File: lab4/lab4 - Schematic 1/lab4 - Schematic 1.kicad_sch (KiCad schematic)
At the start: 6 parts, among them SW1 SW_SPDT

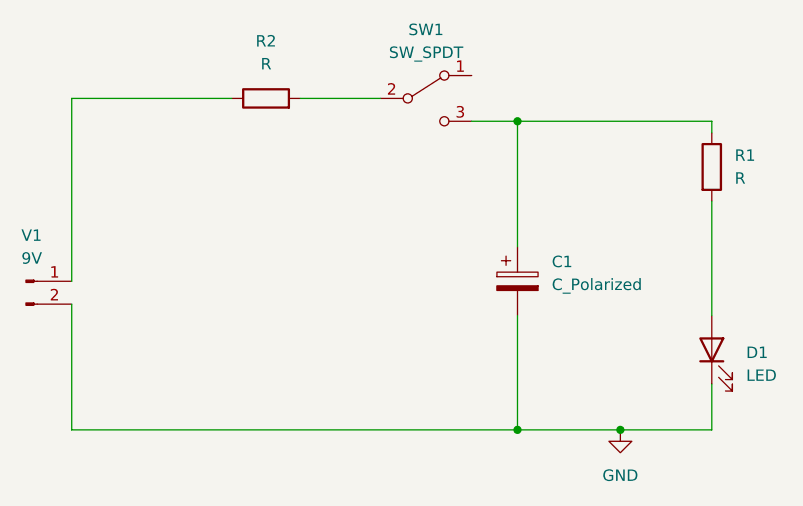
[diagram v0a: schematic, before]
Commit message: PCB for first schematic is complete
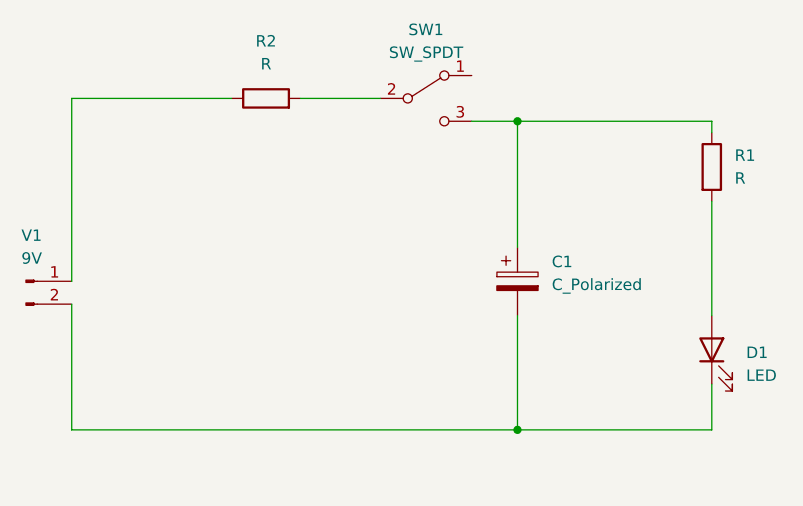
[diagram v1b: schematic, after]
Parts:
- C1: footprint (none) -> Capacitor_THT:C_Radial_D5.0mm_H5.0mm_P2.00mm
- D1: footprint (none) -> LED_THT:LED_D5.0mm
- R1, R2: footprint (none) -> Resistor_THT:R_Axial_DIN0516_L15.5mm_D5.0mm_P20.32mm_Horizontal
- SW1: footprint (none) -> Button_Switch_THT:SW_E-Switch_EG1224_SPDT_Angled
- V1: footprint (none) -> Connector_JST:JST_PH_B2B-PH-K_1x02_P2.00mm_Vertical
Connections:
- net GND: no longer names the net of C1.2, D1.1 (K), V1.2 (Pin_2)
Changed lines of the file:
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@@
   (junction (at 104.14 63.5) (diameter 0) (color 0 0 0 0)
-  )
-  (junction (at 115.57 97.79) (diameter 0) (color 0 0 0 0)
   )
   (wire (pts (xy 54.61 97.79) (xy 104.14 97.79))
@@
     (stroke (width 0) (type default) (color 0 0 0 0))
   )
-  (wire (pts (xy 104.14 97.79) (xy 115.57 97.79))
+  (wire (pts (xy 104.14 97.79) (xy 125.73 97.79))
     (stroke (width 0) (type default) (color 0 0 0 0))
   )
   (wire (pts (xy 80.01 60.96) (xy 88.9 60.96))
-    (stroke (width 0) (type default) (color 0 0 0 0))
-  )
-  (wire (pts (xy 115.57 97.79) (xy 125.73 97.79))
     (stroke (width 0) (type default) (color 0 0 0 0))
   )
@@
       (effects (font (size 1.27 1.27)) (justify left))
     )
-    (property "Footprint" "" (id 2) (at 123.952 68.58 90)
+    (property "Footprint" "Resistor_THT:R_Axial_DIN0516_L15.5mm_D5.0mm_P20.32mm_Horizontal" (id 2) (at 123.952 68.58 90)
       (effects (font (size 1.27 1.27)) hide)
     )
@@
     (property "Reference" "V1" (id 0) (at 50.165 76.2 0))
     (property "Value" "9V" (id 1) (at 50.165 78.74 0))
-    (property "Footprint" "" (id 2) (at 49.53 81.28 0)
+    (property "Footprint" "Connector_JST:JST_PH_B2B-PH-K_1x02_P2.00mm_Vertical" (id 2) (at 49.53 81.28 0)
       (effects (font (size 1.27 1.27)) hide)
     )
@@
       (effects (font (size 1.27 1.27)) (justify left))
     )
-    (property "Footprint" "" (id 2) (at 105.1052 85.09 0)
+    (property "Footprint" "Capacitor_THT:C_Radial_D5.0mm_H5.0mm_P2.00mm" (id 2) (at 105.1052 85.09 0)
       (effects (font (size 1.27 1.27)) hide)
     )
@@
     (property "Reference" "SW1" (id 0) (at 93.98 53.34 0))
     (property "Value" "SW_SPDT" (id 1) (at 93.98 55.88 0))
-    (property "Footprint" "" (id 2) (at 93.98 60.96 0)
+    (property "Footprint" "Button_Switch_THT:SW_E-Switch_EG1224_SPDT_Angled" (id 2) (at 93.98 60.96 0)
       (effects (font (size 1.27 1.27)) hide)
     )
@@
     (property "Reference" "R2" (id 0) (at 76.2 54.61 90))
     (property "Value" "R" (id 1) (at 76.2 57.15 90))
-    (property "Footprint" "" (id 2) (at 76.2 62.738 90)
+    (property "Footprint" "Resistor_THT:R_Axial_DIN0516_L15.5mm_D5.0mm_P20.32mm_Horizontal" (id 2) (at 76.2 62.738 90)
       (effects (font (size 1.27 1.27)) hide)
     )
@@
     (pin "1")
     (pin "2")
-  )
-  (symbol (lib_id "power:GND") (at 115.57 97.79 0) (unit 1)
-    (in_bom yes) (on_board yes)
-    (property "Reference" "#PWR?" (id 0) (at 115.57 104.14 0)
-      (effects (font (size 1.27 1.27)) hide)
-    )
-    (property "Value" "GND" (id 1) (at 115.57 102.87 0))
-    (property "Footprint" "" (id 2) (at 115.57 97.79 0)
-      (effects (font (size 1.27 1.27)) hide)
-    )
-    (property "Datasheet" "" (id 3) (at 115.57 97.79 0)
-      (effects (font (size 1.27 1.27)) hide)
-    )
-    (pin "1")
   )
   (symbol (lib_id "Device:LED") (at 125.73 88.9 90) (unit 1)
@@
       (effects (font (size 1.27 1.27)) (justify right))
     )
-    (property "Footprint" "" (id 2) (at 125.73 88.9 0)
+    (property "Footprint" "LED_THT:LED_D5.0mm" (id 2) (at 125.73 88.9 0)
       (effects (font (size 1.27 1.27)) hide)
     )
@@
   )
   (symbol_instances
-    (path "/c10699f1-2793-4772-84fe-2a656fa5e6fd"
-      (reference "#PWR?") (unit 1) (value "GND") (footprint "")
-    )
     (path "/700b967e-4bff-42e1-aacf-43ca7dfe3977"
-      (reference "C1") (unit 1) (value "C_Polarized") (footprint "")
+      (reference "C1") (unit 1) (value "C_Polarized") (footprint "Capacitor_THT:C_Radial_D5.0mm_H5.0mm_P2.00mm")
     )
     (path "/ee72d974-9b6d-493f-be03-6af7e12d2705"
-      (reference "D1") (unit 1) (value "LED") (footprint "")
+      (reference "D1") (unit 1) (value "LED") (footprint "LED_THT:LED_D5.0mm")
     )
     (path "/154d4432-bc96-4ba0-815c-e76ff5ef6915"
-      (reference "R1") (unit 1) (value "R") (footprint "")
+      (reference "R1") (unit 1) (value "R") (footprint "Resistor_THT:R_Axial_DIN0516_L15.5mm_D5.0mm_P20.32mm_Horizontal")
     )
     (path "/9a4560ba-a4e4-42ca-868e-2d73b9619cef"
-      (reference "R2") (unit 1) (value "R") (footprint "")
+      (reference "R2") (unit 1) (value "R") (footprint "Resistor_THT:R_Axial_DIN0516_L15.5mm_D5.0mm_P20.32mm_Horizontal")
     )
     (path "/8f077c62-ae1c-439f-9bb5-1859286f71e7"
-      (reference "SW1") (unit 1) (value "SW_SPDT") (footprint "")
+      (reference "SW1") (unit 1) (value "SW_SPDT") (footprint "Button_Switch_THT:SW_E-Switch_EG1224_SPDT_Angled")
     )
     (path "/56201865-dbf7-4f6d-94d7-fd3e7dfba9fa"
-      (reference "V1") (unit 1) (value "9V") (footprint "")
+      (reference "V1") (unit 1) (value "9V") (footprint "Connector_JST:JST_PH_B2B-PH-K_1x02_P2.00mm_Vertical")
     )
   )
